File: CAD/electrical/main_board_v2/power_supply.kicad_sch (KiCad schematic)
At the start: 19 parts

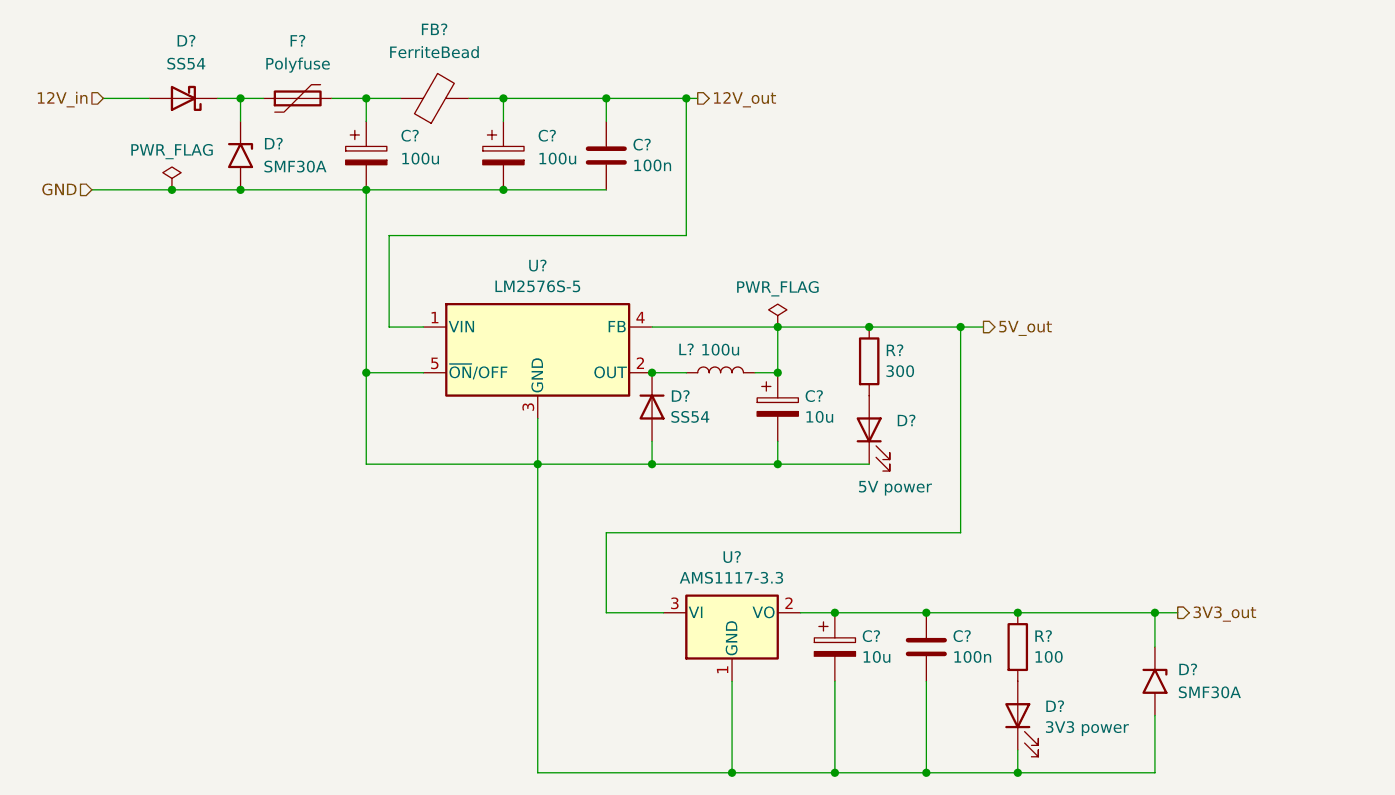
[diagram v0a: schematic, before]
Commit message: Updated version of motor board and main board
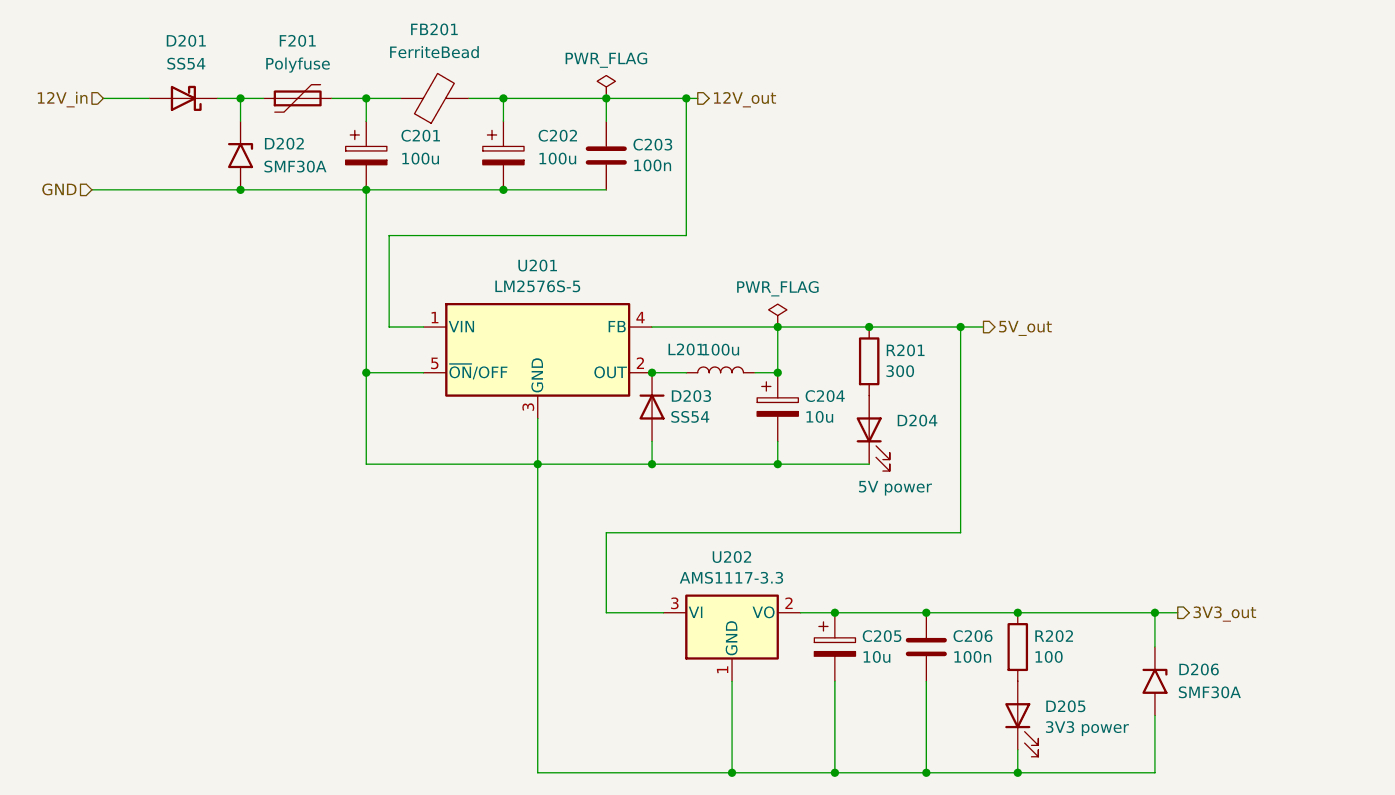
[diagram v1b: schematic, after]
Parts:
- C201, C202: renamed from C?; footprint (none) -> Capacitor_THT:CP_Radial_D10.0mm_P5.00mm
- D201: renamed from D?; footprint (none) -> Diode_SMD:D_SMA
- F201: renamed from F?; footprint (none) -> Fuse:Fuse_1812_4532Metric
- FB201: renamed from FB?; footprint (none) -> Inductor_SMD:L_0805_2012Metric
- gave numbers to parts that had none: 14
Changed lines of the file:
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@@
   (junction (at 92.71 59.69) (diameter 0) (color 0 0 0 0)
   )
-  (junction (at 85.09 69.85) (diameter 0) (color 0 0 0 0)
-  )
   (junction (at 92.71 69.85) (diameter 0) (color 0 0 0 0)
   )
@@
     (stroke (width 0) (type default) (color 0 0 0 0))
   )
-  (wire (pts (xy 76.2 69.85) (xy 85.09 69.85))
-    (stroke (width 0) (type default) (color 0 0 0 0))
-  )
   (wire (pts (xy 77.47 59.69) (xy 82.55 59.69))
     (stroke (width 0) (type default) (color 0 0 0 0))
@@
     (stroke (width 0) (type default) (color 0 0 0 0))
   )
-  (wire (pts (xy 85.09 69.85) (xy 92.71 69.85))
+  (wire (pts (xy 76.2 69.85) (xy 92.71 69.85))
     (stroke (width 0) (type default) (color 0 0 0 0))
   )
@@
     (effects (font (size 1.27 1.27)) (justify left))
   )
+  (symbol (lib_id "power:PWR_FLAG") (at 133.35 59.69 0) (unit 1)
+    (in_bom yes) (on_board yes)
+    (property "Reference" "#FLG0103" (id 0) (at 133.35 57.785 0)
+      (effects (font (size 1.27 1.27)) hide)
+    )
+    (property "Value" "PWR_FLAG" (id 1) (at 133.35 55.2958 0))
+    (property "Footprint" "" (id 2) (at 133.35 59.69 0)
+      (effects (font (size 1.27 1.27)) hide)
+    )
+    (property "Datasheet" "~" (id 3) (at 133.35 59.69 0)
+      (effects (font (size 1.27 1.27)) hide)
+    )
+    (pin "1")
+  )
   (symbol (lib_id "Device:LED") (at 162.56 96.52 90) (unit 1)
     (in_bom yes) (on_board yes)
-    (property "Reference" "D?" (id 0) (at 165.5572 95.5294 90)
+    (property "Reference" "D204" (id 0) (at 165.5572 95.5294 90)
       (effects (font (size 1.27 1.27)) (justify right))
     )
@@
   (symbol (lib_id "Device:C_Polarized") (at 106.68 66.04 0) (unit 1)
     (in_bom yes) (on_board yes) (fields_autoplaced)
-    (property "Reference" "C?" (id 0) (at 110.49 63.8809 0)
+    (property "Reference" "C201" (id 0) (at 110.49 63.8809 0)
       (effects (font (size 1.27 1.27)) (justify left))
     )
@@
       (effects (font (size 1.27 1.27)) (justify left))
     )
-    (property "Footprint" "" (id 2) (at 107.6452 69.85 0)
+    (property "Footprint" "Capacitor_THT:CP_Radial_D10.0mm_P5.00mm" (id 2) (at 107.6452 69.85 0)
       (effects (font (size 1.27 1.27)) hide)
     )
@@
   (symbol (lib_id "power:PWR_FLAG") (at 152.4 85.09 0) (unit 1)
     (in_bom yes) (on_board yes)
-    (property "Reference" "#FLG?" (id 0) (at 152.4 83.185 0)
+    (property "Reference" "#FLG0101" (id 0) (at 152.4 83.185 0)
       (effects (font (size 1.27 1.27)) hide)
     )
@@
   (symbol (lib_id "main_board-rescue:CP-Device") (at 152.4 93.98 0) (unit 1)
     (in_bom yes) (on_board yes)
-    (property "Reference" "C?" (id 0) (at 155.3972 92.8116 0)
+    (property "Reference" "C204" (id 0) (at 155.3972 92.8116 0)
       (effects (font (size 1.27 1.27)) (justify left))
     )
@@
   (symbol (lib_id "Regulator_Linear:AMS1117-3.3") (at 147.32 116.84 0) (unit 1)
     (in_bom yes) (on_board yes)
-    (property "Reference" "U?" (id 0) (at 147.32 110.6932 0))
+    (property "Reference" "U202" (id 0) (at 147.32 110.6932 0))
     (property "Value" "AMS1117-3.3" (id 1) (at 147.32 113.0046 0))
     (property "Footprint" "Package_TO_SOT_SMD:SOT-223-3_TabPin2" (id 2) (at 147.32 111.76 0)
@@
   (symbol (lib_id "Device:D_Schottky") (at 86.36 59.69 180) (unit 1)
     (in_bom yes) (on_board yes) (fields_autoplaced)
-    (property "Reference" "D?" (id 0) (at 86.6775 53.34 0))
+    (property "Reference" "D201" (id 0) (at 86.6775 53.34 0))
     (property "Value" "SS54" (id 1) (at 86.6775 55.88 0))
-    (property "Footprint" "" (id 2) (at 86.36 59.69 0)
+    (property "Footprint" "Diode_SMD:D_SMA" (id 2) (at 86.36 59.69 0)
       (effects (font (size 1.27 1.27)) hide)
     )
@@
     (pin "2")
   )
-  (symbol (lib_id "power:PWR_FLAG") (at 85.09 69.85 0) (unit 1)
-    (in_bom yes) (on_board yes)
-    (property "Reference" "#FLG?" (id 0) (at 85.09 67.945 0)
-      (effects (font (size 1.27 1.27)) hide)
-    )
-    (property "Value" "PWR_FLAG" (id 1) (at 85.09 65.4558 0))
-    (property "Footprint" "" (id 2) (at 85.09 69.85 0)
-      (effects (font (size 1.27 1.27)) hide)
-    )
-    (property "Datasheet" "~" (id 3) (at 85.09 69.85 0)
-      (effects (font (size 1.27 1.27)) hide)
-    )
-    (pin "1")
-  )
   (symbol (lib_id "Device:D") (at 138.43 93.98 270) (unit 1)
     (in_bom yes) (on_board yes)
-    (property "Reference" "D?" (id 0) (at 140.462 92.8116 90)
+    (property "Reference" "D203" (id 0) (at 140.462 92.8116 90)
       (effects (font (size 1.27 1.27)) (justify left))
     )
@@
   (symbol (lib_id "Diode:SMF30A") (at 194.31 124.46 270) (unit 1)
     (in_bom yes) (on_board yes) (fields_autoplaced)
-    (property "Reference" "D?" (id 0) (at 196.85 123.1899 90)
+    (property "Reference" "D206" (id 0) (at 196.85 123.1899 90)
       (effects (font (size 1.27 1.27)) (justify left))
     )
@@
   (symbol (lib_id "Device:R") (at 179.07 120.65 0) (unit 1)
     (in_bom yes) (on_board yes)
-    (property "Reference" "R?" (id 0) (at 180.848 119.4816 0)
+    (property "Reference" "R202" (id 0) (at 180.848 119.4816 0)
       (effects (font (size 1.27 1.27)) (justify left))
     )
@@
   (symbol (lib_id "Device:C") (at 133.35 66.04 0) (unit 1)
     (in_bom yes) (on_board yes)
-    (property "Reference" "C?" (id 0) (at 136.271 64.8716 0)
+    (property "Reference" "C203" (id 0) (at 136.271 64.8716 0)
       (effects (font (size 1.27 1.27)) (justify left))
     )
@@
   (symbol (lib_id "Device:Polyfuse") (at 99.06 59.69 90) (unit 1)
     (in_bom yes) (on_board yes) (fields_autoplaced)
-    (property "Reference" "F?" (id 0) (at 99.06 53.34 90))
+    (property "Reference" "F201" (id 0) (at 99.06 53.34 90))
     (property "Value" "Polyfuse" (id 1) (at 99.06 55.88 90))
-    (property "Footprint" "" (id 2) (at 104.14 58.42 0)
+    (property "Footprint" "Fuse:Fuse_1812_4532Metric" (id 2) (at 104.14 58.42 0)
       (effects (font (size 1.27 1.27)) (justify left) hide)
     )
@@
   (symbol (lib_id "Diode:SMF30A") (at 92.71 66.04 270) (unit 1)
     (in_bom yes) (on_board yes) (fields_autoplaced)
-    (property "Reference" "D?" (id 0) (at 95.25 64.7699 90)
+    (property "Reference" "D202" (id 0) (at 95.25 64.7699 90)
       (effects (font (size 1.27 1.27)) (justify left))
     )
@@
   (symbol (lib_id "Device:C_Polarized") (at 121.92 66.04 0) (unit 1)
     (in_bom yes) (on_board yes) (fields_autoplaced)
-    (property "Reference" "C?" (id 0) (at 125.73 63.8809 0)
+    (property "Reference" "C202" (id 0) (at 125.73 63.8809 0)
       (effects (font (size 1.27 1.27)) (justify left))
     )
@@
       (effects (font (size 1.27 1.27)) (justify left))
     )
-    (property "Footprint" "" (id 2) (at 122.8852 69.85 0)
+    (property "Footprint" "Capacitor_THT:CP_Radial_D10.0mm_P5.00mm" (id 2) (at 122.8852 69.85 0)
       (effects (font (size 1.27 1.27)) hide)
     )
@@
   (symbol (lib_id "main_board-rescue:CP-Device") (at 158.75 120.65 0) (unit 1)
     (in_bom yes) (on_board yes)
-    (property "Reference" "C?" (id 0) (at 161.7472 119.4816 0)
+    (property "Reference" "C205" (id 0) (at 161.7472 119.4816 0)
       (effects (font (size 1.27 1.27)) (justify left))
     )
@@
   (symbol (lib_id "Regulator_Switching:LM2576S-5") (at 125.73 87.63 0) (unit 1)
     (in_bom yes) (on_board yes)
-    (property "Reference" "U?" (id 0) (at 125.73 78.3082 0))
+    (property "Reference" "U201" (id 0) (at 125.73 78.3082 0))
     (property "Value" "LM2576S-5" (id 1) (at 125.73 80.6196 0))
     (property "Footprint" "Package_TO_SOT_SMD:TO-263-5_TabPin3" (id 2) (at 125.73 93.98 0)
@@
   (symbol (lib_id "Device:L") (at 146.05 90.17 90) (unit 1)
     (in_bom yes) (on_board yes)
-    (property "Reference" "L?" (id 0) (at 142.24 87.63 90))
+    (property "Reference" "L201" (id 0) (at 142.24 87.63 90))
     (property "Value" "100u" (id 1) (at 146.05 87.6554 90))
     (property "Footprint" "Inductor_SMD:L_12x12mm_H6mm" (id 2) (at 146.05 90.17 0)
@@
   (symbol (lib_id "Device:R") (at 162.56 88.9 0) (unit 1)
     (in_bom yes) (on_board yes)
-    (property "Reference" "R?" (id 0) (at 164.338 87.7316 0)
+    (property "Reference" "R201" (id 0) (at 164.338 87.7316 0)
       (effects (font (size 1.27 1.27)) (justify left))
     )
@@
   (symbol (lib_id "Device:FerriteBead") (at 114.3 59.69 90) (unit 1)
     (in_bom yes) (on_board yes) (fields_autoplaced)
-    (property "Reference" "FB?" (id 0) (at 114.2492 52.07 90))
+    (property "Reference" "FB201" (id 0) (at 114.2492 52.07 90))
     (property "Value" "FerriteBead" (id 1) (at 114.2492 54.61 90))
-    (property "Footprint" "" (id 2) (at 114.3 61.468 90)
+    (property "Footprint" "Inductor_SMD:L_0805_2012Metric" (id 2) (at 114.3 61.468 90)
       (effects (font (size 1.27 1.27)) hide)
     )
@@
   (symbol (lib_id "Device:C") (at 168.91 120.65 0) (unit 1)
     (in_bom yes) (on_board yes)
-    (property "Reference" "C?" (id 0) (at 171.831 119.4816 0)
+    (property "Reference" "C206" (id 0) (at 171.831 119.4816 0)
       (effects (font (size 1.27 1.27)) (justify left))
     )
@@
   (symbol (lib_id "Device:LED") (at 179.07 128.27 90) (unit 1)
     (in_bom yes) (on_board yes)
-    (property "Reference" "D?" (id 0) (at 182.0672 127.2794 90)
+    (property "Reference" "D205" (id 0) (at 182.0672 127.2794 90)
       (effects (font (size 1.27 1.27)) (justify right))
     )

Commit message: Kicad CAD for mainboard and motorboard (final)
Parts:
- added C1: 100u, Capacitor_SMD:CP_Elec_8x10, symbol Device:C_Polarized
- added C2: 100n, Capacitor_SMD:C_0805_2012Metric, symbol Device:C
- added L1: 10u, Inductor_SMD:L_12x12mm_H6mm, symbol Device:L
- C201, C202: footprint Capacitor_THT:CP_Radial_D10.0mm_P5.00mm -> Capacitor_SMD:CP_Elec_8x10
- C204: value 10u -> 2000u; footprint Capacitor_THT:CP_Radial_D6.3mm_P2.50mm -> Capacitor_SMD:CP_Elec_10x10.5
- C205: value 10u -> 100u; footprint Capacitor_THT:CP_Radial_D6.3mm_P2.50mm -> Capacitor_SMD:CP_Elec_8x10
- R201: value 300 -> 470
- R202: value 100 -> 470
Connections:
- net 5V_out: now also C1.1, C2.1, L1.2; no longer C204.1, L201.2, U201.4 (FB)
- net GND: now also C1.2, C2.2
- new net: C204.1, L1.1, L201.2, U201.4 (FB)
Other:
- moved on the sheet: D204, R201

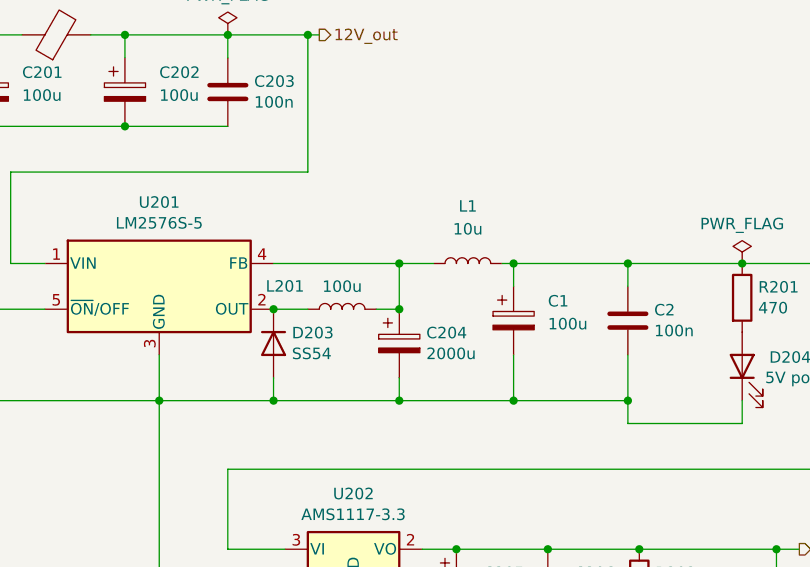
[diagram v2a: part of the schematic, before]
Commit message: LD06 board colplet
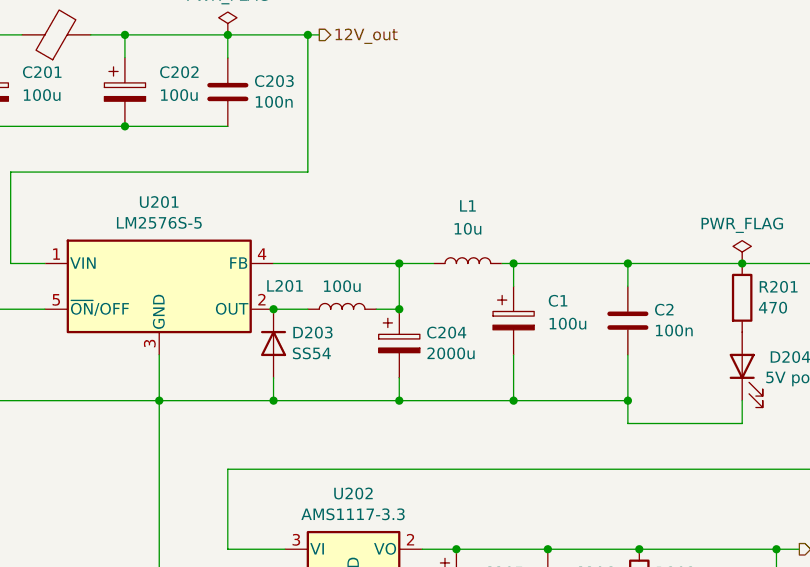
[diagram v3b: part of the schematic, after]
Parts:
- C1, C201, C202, C205: LCSC (none) -> C16133
- C204: LCSC (none) -> C10752
- D202, D206: LCSC (none) -> C19077518
- D204, D205: LCSC C72038 -> C2286
